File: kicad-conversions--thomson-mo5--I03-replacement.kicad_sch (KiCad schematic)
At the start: 3 parts, among them U1 HM7603_32×8_PROM_THREE-STATE_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, U2 HIGH_PERFORMANCE_E2_CMOS_PLD_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

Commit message: assign footprint to capacitor
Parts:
- C1: footprint (none) -> commons-passives_THT:Passive_THT_capacitor_mlcc_W2.54mm_L5.08mm
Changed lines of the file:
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@@
       (effects (font (size 1.27 1.27)) (justify left))
     )
-    (property "Footprint" "" (at 165.1 139.7 0)
+    (property "Footprint" "commons-passives_THT:Passive_THT_capacitor_mlcc_W2.54mm_L5.08mm" (at 165.1 139.7 0)
       (effects (font (size 1.27 1.27)) hide)
     )

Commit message: done wiring
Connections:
- net GND: now reaches C1.2, U1.8 (GND), U2.1 (I/CLK), U2.10 (GND), U2.2 (I), U2.8 (I), U2.9 (I)
- net VCC: now reaches C1.1, U1.16 (VCC), U2.20 (VCC)
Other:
- note added: "Récupérer C22 de la carte-mère et le placer en C1"
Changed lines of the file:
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@@
     (stroke (width 0) (type default))
+  )
+  (text "Récupérer C22 de\nla carte-mère et\nle placer en C1" (at 166.37 135.89 0)
+    (effects (font (size 1.27 1.27)) (justify left bottom))
   )
   (label "O6" (at 83.82 101.6 0) (fields_autoplaced)
@@
   (label "O1" (at 83.82 88.9 0) (fields_autoplaced)
     (effects (font (size 1.27 1.27)) (justify left bottom))
+  )
+  (label "GND" (at 83.82 106.68 180) (fields_autoplaced)
+    (effects (font (size 1.27 1.27)) (justify right bottom))
   )
   (label "~{CE}" (at 132.08 91.44 180) (fields_autoplaced)
@@
     (effects (font (size 1.27 1.27)) (justify right bottom))
   )
+  (label "VCC" (at 132.08 88.9 0) (fields_autoplaced)
+    (effects (font (size 1.27 1.27)) (justify left bottom))
+  )
   (label "~{CE}" (at 134.62 149.86 180) (fields_autoplaced)

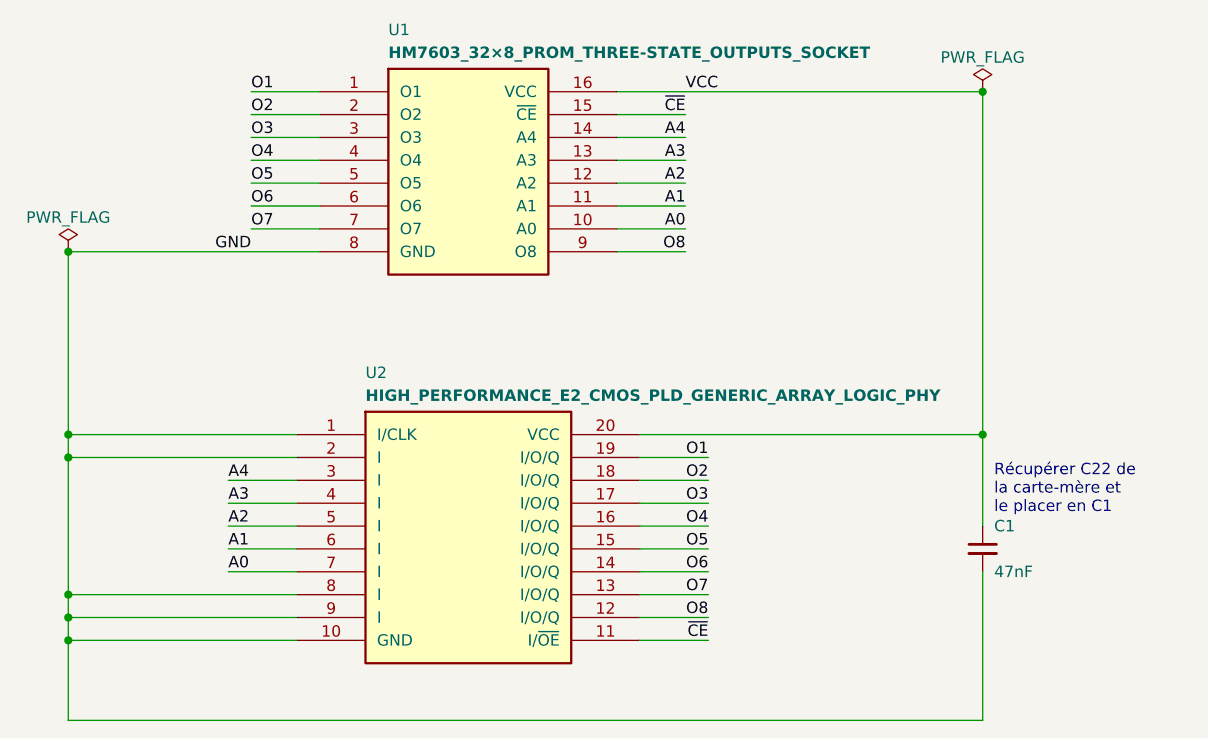
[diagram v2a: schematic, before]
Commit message: schematic -- rename wires with functionnal names
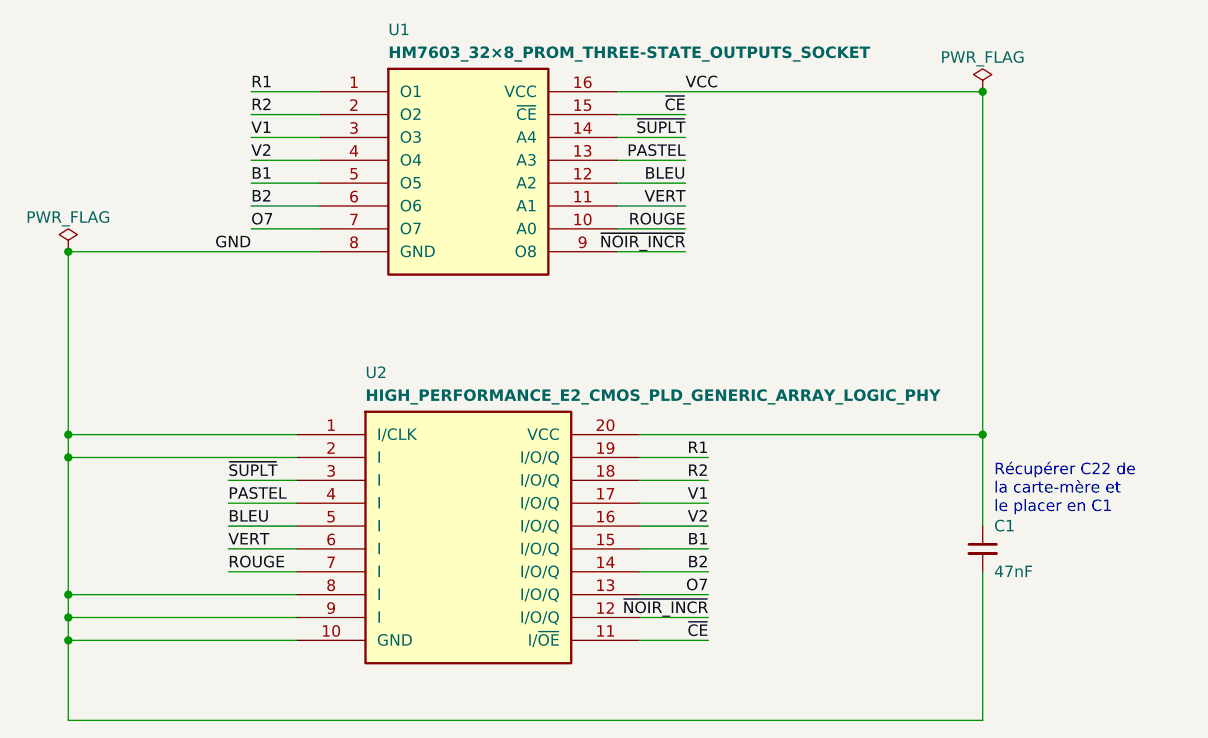
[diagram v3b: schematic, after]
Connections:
- net A0 renamed ROUGE
- net A1 renamed VERT
- net A2 renamed BLEU
- net A3 renamed PASTEL
- net A4 renamed ~{SUPLT}
- net O1 renamed R1
- net O2 renamed R2
- net O3 renamed V1
- net O4 renamed V2
- net O5 renamed B1
- net O6 renamed B2
- net O8 renamed ~{NOIR_INCR}
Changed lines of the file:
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@@
     (effects (font (size 1.27 1.27)) (justify left bottom))
   )
-  (label "O6" (at 83.82 101.6 0) (fields_autoplaced)
+  (label "B2" (at 83.82 101.6 0) (fields_autoplaced)
     (effects (font (size 1.27 1.27)) (justify left bottom))
   )
-  (label "A0" (at 132.08 104.14 180) (fields_autoplaced)
+  (label "ROUGE" (at 132.08 104.14 180) (fields_autoplaced)
     (effects (font (size 1.27 1.27)) (justify right bottom))
   )
-  (label "O8" (at 134.62 147.32 180) (fields_autoplaced)
+  (label "~{NOIR_INCR}" (at 134.62 147.32 180) (fields_autoplaced)
     (effects (font (size 1.27 1.27)) (justify right bottom))
   )
-  (label "O1" (at 83.82 88.9 0) (fields_autoplaced)
+  (label "R1" (at 83.82 88.9 0) (fields_autoplaced)
     (effects (font (size 1.27 1.27)) (justify left bottom))
   )
@@
     (effects (font (size 1.27 1.27)) (justify left bottom))
   )
-  (label "A0" (at 81.28 142.24 0) (fields_autoplaced)
+  (label "ROUGE" (at 81.28 142.24 0) (fields_autoplaced)
     (effects (font (size 1.27 1.27)) (justify left bottom))
   )
-  (label "A4" (at 132.08 93.98 180) (fields_autoplaced)
+  (label "~{SUPLT}" (at 132.08 93.98 180) (fields_autoplaced)
     (effects (font (size 1.27 1.27)) (justify right bottom))
   )
-  (label "O3" (at 134.62 134.62 180) (fields_autoplaced)
+  (label "V1" (at 134.62 134.62 180) (fields_autoplaced)
     (effects (font (size 1.27 1.27)) (justify right bottom))
   )
-  (label "A3" (at 132.08 96.52 180) (fields_autoplaced)
+  (label "PASTEL" (at 132.08 96.52 180) (fields_autoplaced)
     (effects (font (size 1.27 1.27)) (justify right bottom))
   )
-  (label "A3" (at 81.28 134.62 0) (fields_autoplaced)
+  (label "PASTEL" (at 81.28 134.62 0) (fields_autoplaced)
     (effects (font (size 1.27 1.27)) (justify left bottom))
   )
-  (label "O2" (at 134.62 132.08 180) (fields_autoplaced)
+  (label "R2" (at 134.62 132.08 180) (fields_autoplaced)
     (effects (font (size 1.27 1.27)) (justify right bottom))
   )
-  (label "O5" (at 134.62 139.7 180) (fields_autoplaced)
+  (label "B1" (at 134.62 139.7 180) (fields_autoplaced)
     (effects (font (size 1.27 1.27)) (justify right bottom))
   )
-  (label "A2" (at 81.28 137.16 0) (fields_autoplaced)
+  (label "BLEU" (at 81.28 137.16 0) (fields_autoplaced)
     (effects (font (size 1.27 1.27)) (justify left bottom))
   )
-  (label "O4" (at 134.62 137.16 180) (fields_autoplaced)
+  (label "V2" (at 134.62 137.16 180) (fields_autoplaced)
     (effects (font (size 1.27 1.27)) (justify right bottom))
   )
@@
     (effects (font (size 1.27 1.27)) (justify right bottom))
   )
-  (label "A2" (at 132.08 99.06 180) (fields_autoplaced)
+  (label "BLEU" (at 132.08 99.06 180) (fields_autoplaced)
     (effects (font (size 1.27 1.27)) (justify right bottom))
   )
-  (label "O6" (at 134.62 142.24 180) (fields_autoplaced)
+  (label "B2" (at 134.62 142.24 180) (fields_autoplaced)
     (effects (font (size 1.27 1.27)) (justify right bottom))
   )
-  (label "O5" (at 83.82 99.06 0) (fields_autoplaced)
+  (label "B1" (at 83.82 99.06 0) (fields_autoplaced)
     (effects (font (size 1.27 1.27)) (justify left bottom))
   )
-  (label "O3" (at 83.82 93.98 0) (fields_autoplaced)
+  (label "V1" (at 83.82 93.98 0) (fields_autoplaced)
     (effects (font (size 1.27 1.27)) (justify left bottom))
   )
-  (label "A1" (at 81.28 139.7 0) (fields_autoplaced)
+  (label "VERT" (at 81.28 139.7 0) (fields_autoplaced)
     (effects (font (size 1.27 1.27)) (justify left bottom))
   )
-  (label "A1" (at 132.08 101.6 180) (fields_autoplaced)
+  (label "VERT" (at 132.08 101.6 180) (fields_autoplaced)
     (effects (font (size 1.27 1.27)) (justify right bottom))
   )
-  (label "O1" (at 134.62 129.54 180) (fields_autoplaced)
+  (label "R1" (at 134.62 129.54 180) (fields_autoplaced)
     (effects (font (size 1.27 1.27)) (justify right bottom))
   )
-  (label "O2" (at 83.82 91.44 0) (fields_autoplaced)
+  (label "R2" (at 83.82 91.44 0) (fields_autoplaced)
     (effects (font (size 1.27 1.27)) (justify left bottom))
   )
-  (label "A4" (at 81.28 132.08 0) (fields_autoplaced)
+  (label "~{SUPLT}" (at 81.28 132.08 0) (fields_autoplaced)
     (effects (font (size 1.27 1.27)) (justify left bottom))
   )
-  (label "O4" (at 83.82 96.52 0) (fields_autoplaced)
+  (label "V2" (at 83.82 96.52 0) (fields_autoplaced)
     (effects (font (size 1.27 1.27)) (justify left bottom))
   )
-  (label "O8" (at 132.08 106.68 180) (fields_autoplaced)
+  (label "~{NOIR_INCR}" (at 132.08 106.68 180) (fields_autoplaced)
     (effects (font (size 1.27 1.27)) (justify right bottom))
   )

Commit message: added proper description in schematic, pcb
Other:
- company: (none) -> Sporniket
- title: (none) -> Replacement of I03 (color PROM) for the Thomson MO5
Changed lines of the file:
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@@
   (paper "A4" portrait)
   (title_block
+    (title "Replacement of I03 (color PROM) for the Thomson MO5")
     (date "2024-11-03")
+    (rev "v1.0.0-draft")
+    (company "Sporniket")
+    (comment 3 "https://github.com/sporniket/kicad-conversions--thomson-mo5--i03-replacement")
+    (comment 4 "Original repository:")
   )
   (junction (at 63.5 149.86) (diameter 0) (color 0 0 0 0)
